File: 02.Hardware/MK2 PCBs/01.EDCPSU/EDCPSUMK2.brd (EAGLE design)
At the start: 96 x 60.8 mm, 180 parts, among them J1 DX07S016JA1R1500, J3 AVR_ISP, J4 FTDI_DEVICE, J6 Display, K1 FLEX8, Q2 2N7002PW, Q4 2N7002PW, Q5 2N7002PW, Q9 2N7002PW, U1 ATMEGA328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

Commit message: Planos modificados
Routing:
- net VCC-ISO: track 139.6 -> 126.8 mm, vias 20 -> 21
- net VCC: track 73.0 -> 74.5 mm, vias 8 -> 9
- net IN_OVC: track 160.0 -> 158.5 mm, vias 3 -> 4
- net SEL: track 78.9 -> 80.0 mm, vias 3 -> 4
- net GND: track 204.7 -> 205.4 mm

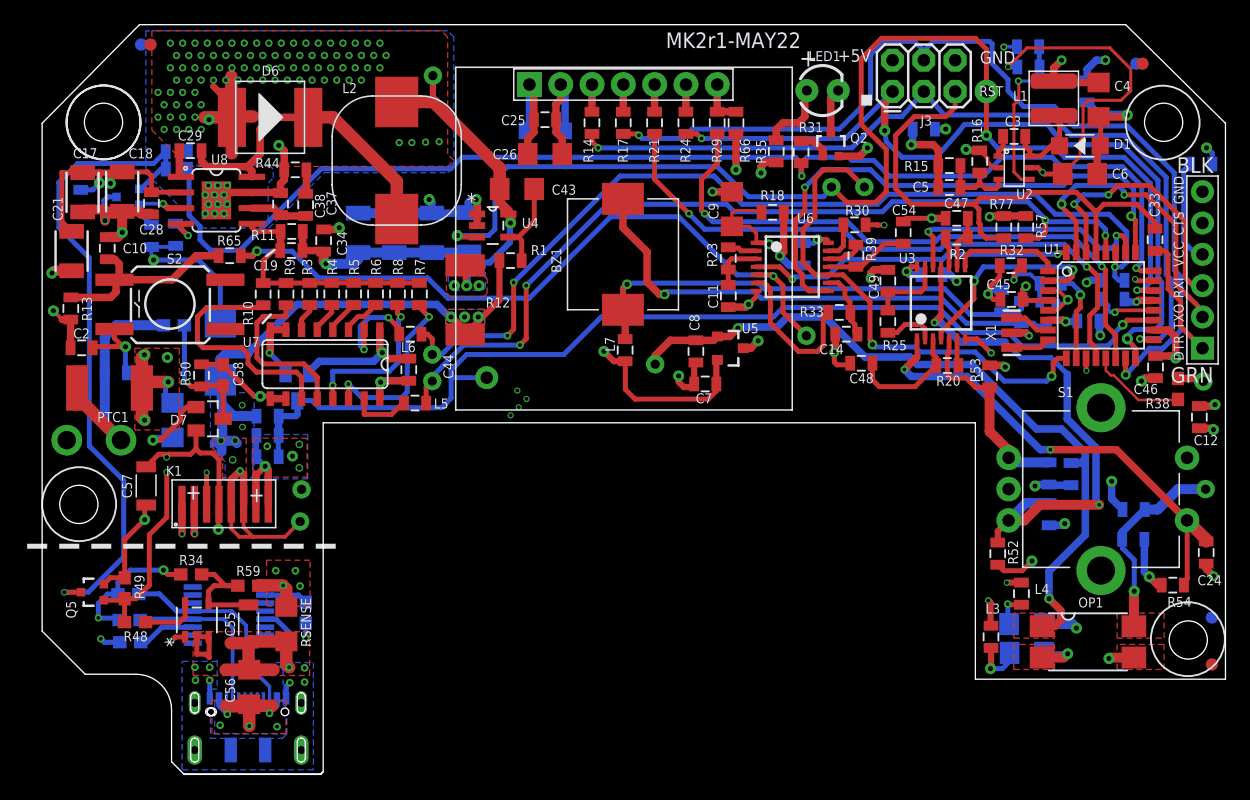
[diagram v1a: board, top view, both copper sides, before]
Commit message: Update PCB ECPSUMK2
Actualizacion y mejora de las capas de PWR y GND
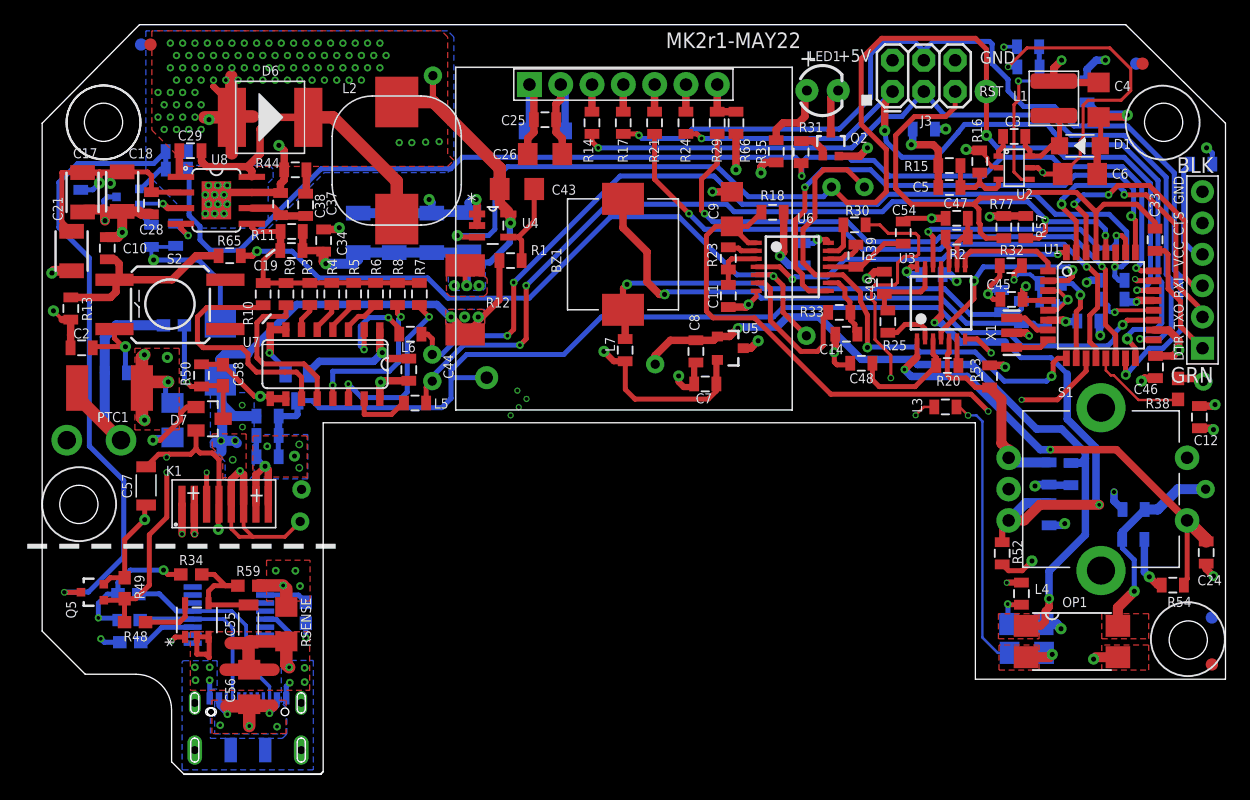
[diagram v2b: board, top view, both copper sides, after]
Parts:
- TP2: value (none) -> VCCIO
- TP5: value (none) -> PEDAL
- moved L3 19.0 mm to (88.1, 41.8), turned to 0 degrees
- moved OP1 1.30 mm to (98.3, 22.8)
- moved R52 0.36 mm to (92.7, 29.9)
- moved C49 0.32 mm to (83.1, 51.9)
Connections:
- net N$31 renamed PEDAL
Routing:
- net IN_OVC: track 158.5 -> 98.2 mm
- net PEDAL+: track 91.1 -> 70.5 mm
- net SPARE: track 75.4 -> 54.8 mm
- net N$43: track 4.17 -> 22.8 mm
- net GND: track 205.4 -> 203.8 mm
- net N$41: track 4.13 -> 2.90 mm
- net VCC-ISO: track 126.8 -> 126.1 mm
- net PEDAL: track 16.3 -> 16.8 mm
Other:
- board text added: "ISENSE"
- board text added: "PEDAL"
- board text added: "SPARE2"
- board text added: "VOSEN"
- board text added: "VOUT"
- board text removed: "OPTO_OP"
